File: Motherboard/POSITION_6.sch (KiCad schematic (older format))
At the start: 31 parts, among them Q24 MOSFET_N_(2N7002P,215), Q25 MOSFET_N_(2N7002P,215), Q26 MOSFET_N_(FDMA430NZ), Q27 MOSFET_P_(BS250FTA)

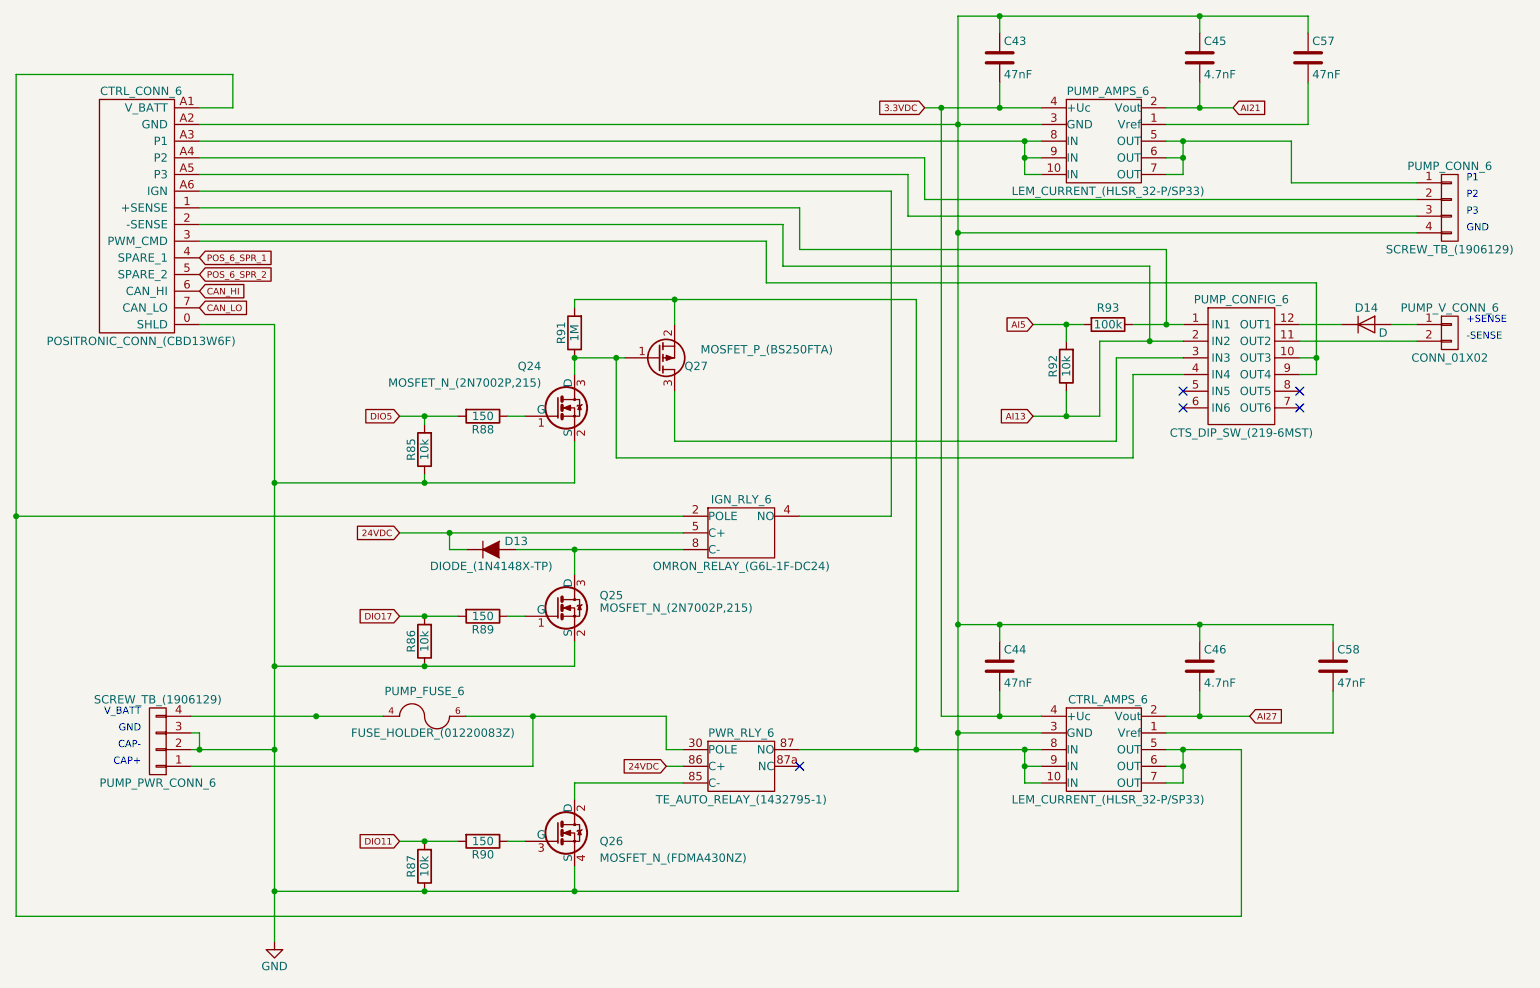
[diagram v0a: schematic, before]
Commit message: - Refer to Google Drive BOM for list of changes for v1.1 - Create drawing for Hella BLDC controller plate.
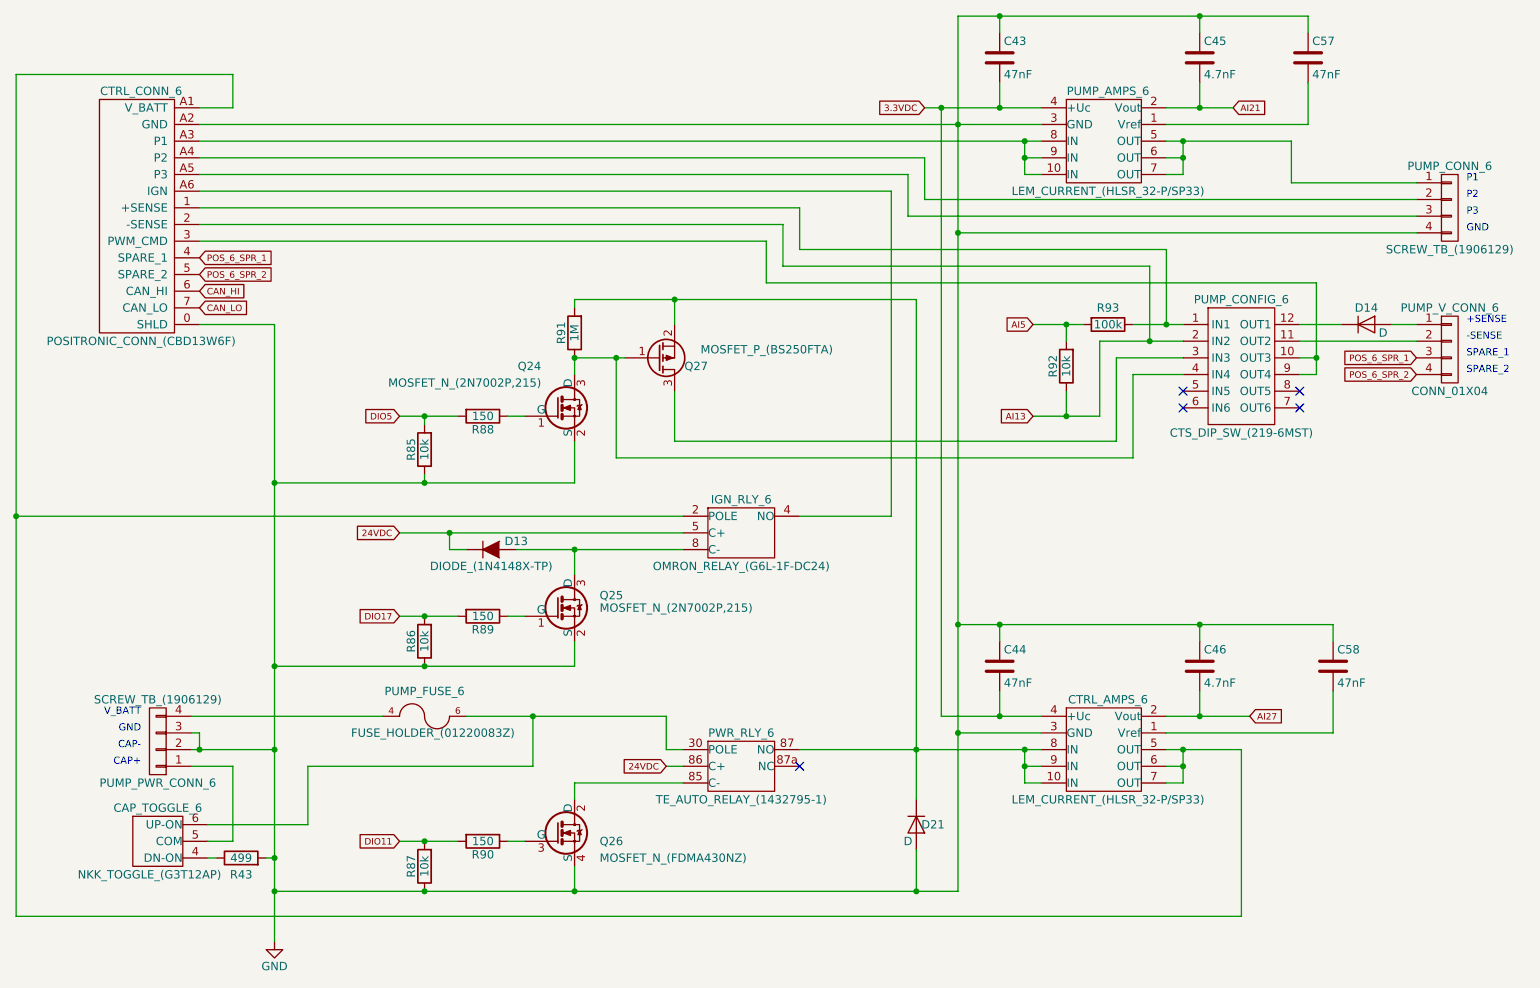
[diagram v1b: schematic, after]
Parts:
- removed PUMP_V_CONN_6: CONN_01X02, Smart_Tank:PHNX_TB_SCREW_2_POS_(1729128), symbol CONN_01X02
- added CAP_TOGGLE_6: NKK_TOGGLE_(G3T12AP), Smart_Tank:NKK_TOGGLE_(G3T12AP), symbol NKK_TOGGLE_(G3T12AP)
- added D21: D, Diodes_SMD:D_SOD-123, symbol D
- added PUMP_V_CONN_6: CONN_01X04, Smart_Tank:PHNX_TB_SCREW_4_POS_(1729144), symbol CONN_01X04
- added R43: 499, Resistors_SMD:R_1206, symbol R
- D14: footprint Diodes_SMD:SOD-523 -> Diodes_SMD:SOD-123
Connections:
- net GND: now also D21.2 (A), R43.2
- net POS_6_SPR_1: now also PUMP_V_CONN_6.3 (P3)
- net POS_6_SPR_2: now also PUMP_V_CONN_6.4 (P4)
- net at PUMP_FUSE_6.6, PUMP_FUSE_6.7, PWR_RLY_6.30 (POLE): now also CAP_TOGGLE_6.6 (UP-ON); no longer PUMP_PWR_CONN_6.1 (P1)
- net at CTRL_AMPS_6.10 (IN), CTRL_AMPS_6.8 (IN), CTRL_AMPS_6.9 (IN)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: now also D21.1 (K)
- net at PUMP_CONFIG_6.11 (OUT2): now also PUMP_V_CONN_6.2 (P2)
- net at D14.2 (A): now also PUMP_V_CONN_6.1 (P1)
- new net: CAP_TOGGLE_6.5 (COM), PUMP_PWR_CONN_6.1 (P1)
- new net: CAP_TOGGLE_6.4 (DN-ON), R43.1
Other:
- note added: "SPARE_1"
- note added: "SPARE_2"
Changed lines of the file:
@@
 CAP+
 $Comp
-L GND #PWR026
+L GND #PWR027
 U 1 1 57A945C3
 P 2950 6350
-F 0 "#PWR026" H 2950 6100 50  0001 C CNN
+F 0 "#PWR027" H 2950 6100 50  0001 C CNN
 F 1 "GND" H 2950 6200 50  0000 C CNN
 F 2 "" H 2950 6350 50  0000 C CNN
@@
 	1    0    0    -1
 $EndComp
-$Comp
-L CONN_01X02 PUMP_V_CONN_6
-U 1 1 57A9467F
-P 10000 2700
-F 0 "PUMP_V_CONN_6" H 10000 2850 50  0000 C CNN
-F 1 "CONN_01X02" H 10000 2550 50  0000 C CNN
-F 2 "Smart_Tank:PHNX_TB_SCREW_2_POS_(1729128)" H 10000 2700 50  0001 C CNN
-F 3 "" H 10000 2700 50  0000 C CNN
-	1    10000 2700
-	1    0    0    -1
-$EndComp
 Text Notes 10100 2650 0    43   ~ 0
 +SENSE
@@
 	2500 5100 2500 5200
 Connection ~ 2500 5200
-Wire Wire Line
-	4500 5300 2450 5300
 Connection ~ 4500 5000
 Wire Wire Line
@@
 	4750 2500 6800 2500
 Wire Wire Line
-	6800 2500 6800 5200
+	6800 2500 6800 5500
 Connection ~ 6800 5200
 Wire Wire Line
@@
 	2950 4700 4750 4700
 Connection ~ 3850 4700
-Connection ~ 3200 5000
 Connection ~ 2950 6050
 Wire Wire Line
@@
 F 0 "D14" H 9500 2750 50  0000 C CNN
 F 1 "D" H 9600 2600 50  0000 C CNN
-F 2 "Diodes_SMD:SOD-523" H 9500 2650 50  0001 C CNN
+F 2 "Diodes_SMD:SOD-123" H 9500 2650 50  0001 C CNN
 F 3 "" H 9500 2650 50  0000 C CNN
 	1    9500 2650
@@
 	9300 4450 9300 4550
 Connection ~ 8500 4450
+$Comp
+L NKK_TOGGLE_(G3T12AP) CAP_TOGGLE_6
+U 1 1 5976DF6C
+P 2250 5750
+F 0 "CAP_TOGGLE_6" H 2250 5950 50  0000 C CNN
+F 1 "NKK_TOGGLE_(G3T12AP)" H 2200 5550 50  0000 C CNN
+F 2 "Smart_Tank:NKK_TOGGLE_(G3T12AP)" H 2250 4550 50  0001 C CNN
+F 3 "" H 2250 4550 50  0000 C CNN
+	1    2250 5750
+	1    0    0    -1
+$EndComp
+Wire Wire Line
+	2450 5300 2700 5300
+Wire Wire Line
+	3150 5300 4500 5300
+$Comp
+L D D21
+U 1 1 5976EE02
+P 6800 5650
+F 0 "D21" V 6800 5750 50  0000 C CNN
+F 1 "D" V 6900 5600 50  0000 C CNN
+F 2 "Diodes_SMD:D_SOD-123" H 6800 5650 50  0001 C CNN
+F 3 "" H 6800 5650 50  0000 C CNN
+	1    6800 5650
+	0    1    1    0
+$EndComp
+Wire Wire Line
+	6800 5800 6800 6050
+Connection ~ 6800 6050
+$Comp
+L R R43
+U 1 1 5978DEAB
+P 2750 5850
+F 0 "R43" V 2650 5850 50  0000 C CNN
+F 1 "499" V 2750 5850 50  0000 C CNN
+F 2 "Resistors_SMD:R_1206" V 2680 5850 50  0001 C CNN
+F 3 "" H 2750 5850 50  0000 C CNN
+	1    2750 5850
+	0    -1   -1   0
+$EndComp
+Wire Wire Line
+	2550 5750 2700 5750
+Wire Wire Line
+	2700 5750 2700 5300
+Wire Wire Line
+	2550 5650 3150 5650
+Wire Wire Line
+	3150 5650 3150 5300
+Wire Wire Line
+	2600 5850 2550 5850
+Wire Wire Line
+	2900 5850 2950 5850
+Connection ~ 2950 5850
+$Comp
+L CONN_01X04 PUMP_V_CONN_6
+U 1 1 5979C896
+P 10000 2800
+F 0 "PUMP_V_CONN_6" H 10000 3050 50  0000 C CNN
+F 1 "CONN_01X04" H 10000 2550 50  0000 C CNN
+F 2 "Smart_Tank:PHNX_TB_SCREW_4_POS_(1729144)" H 10000 2800 50  0001 C CNN
+F 3 "" H 10000 2800 50  0001 C CNN
+	1    10000 2800
+	1    0    0    -1
+$EndComp
+Text GLabel 9800 2850 0    39   Input ~ 0
+POS_6_SPR_1
+Text GLabel 9800 2950 0    39   Input ~ 0
+POS_6_SPR_2
+Text Notes 10100 2850 0    43   ~ 0
+SPARE_1
+Text Notes 10100 2950 0    43   ~ 0
+SPARE_2
 $EndSCHEMATC

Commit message: - Created Modbus Adapter.
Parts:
- C43, C44, C45, C46, C57, C58: symbol C -> Smart-Tank-Motherboard-rescue:C
- CAP_TOGGLE_6: symbol NKK_TOGGLE_(G3T12AP) -> Smart-Tank-Motherboard-rescue:NKK_TOGGLE_(G3T12AP)
- CTRL_AMPS_6, PUMP_AMPS_6: symbol LEM_CURRENT_(HLSR_32-P/SP33) -> Smart-Tank-Motherboard-rescue:LEM_CURRENT_(HLSR_32-P_SP33)
- CTRL_CONN_6: symbol POSITRONIC_CONN_(CBD13W6F) -> Smart-Tank-Motherboard-rescue:POSITRONIC_CONN_(CBD13W6F)
- D13: symbol DIODE_(1N4148X-TP) -> Smart-Tank-Motherboard-rescue:DIODE_(1N4148X-TP)
- D14, D21: symbol D -> Smart-Tank-Motherboard-rescue:D
- IGN_RLY_6: symbol OMRON_RELAY_(G6L-1F-DC24) -> Smart-Tank-Motherboard-rescue:OMRON_RELAY_(G6L-1F-DC24)
- PUMP_CONFIG_6: symbol CTS_DIP_SW_(219-6MST) -> Smart-Tank-Motherboard-rescue:CTS_DIP_SW_(219-6MST)
- PUMP_CONN_6, PUMP_PWR_CONN_6: symbol SCREW_TB_(1906129) -> Smart-Tank-Motherboard-rescue:SCREW_TB_(1906129)
- PUMP_FUSE_6: symbol FUSE_HOLDER_(01220083Z) -> Smart-Tank-Motherboard-rescue:FUSE_HOLDER_(01220083Z)
- PUMP_V_CONN_6: symbol CONN_01X04 -> Smart-Tank-Motherboard-rescue:CONN_01X04
- PWR_RLY_6: symbol TE_AUTO_RELAY_(1432795-1) -> Smart-Tank-Motherboard-rescue:TE_AUTO_RELAY_(1432795-1)
- Q24, Q25: symbol MOSFET_N_(2N7002P,215) -> Smart-Tank-Motherboard-rescue:MOSFET_N_(2N7002P,215)
- Q26: symbol MOSFET_N_(FDMA430NZ) -> Smart-Tank-Motherboard-rescue:MOSFET_N_(FDMA430NZ)
- Q27: symbol MOSFET_P_(BS250FTA) -> Smart-Tank-Motherboard-rescue:MOSFET_P_(BS250FTA)
- R43, R85, R86, R87, R88, R89, R90, R91, R92, R93: symbol R -> Smart-Tank-Motherboard-rescue:R
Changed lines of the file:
@@
-EESchema Schematic File Version 2
-LIBS:Smart Tank Motherboard-rescue
-LIBS:power
-LIBS:device
-LIBS:transistors
-LIBS:conn
-LIBS:linear
-LIBS:regul
-LIBS:74xx
-LIBS:cmos4000
-LIBS:adc-dac
-LIBS:memory
-LIBS:xilinx
-LIBS:microcontrollers
-LIBS:dsp
-LIBS:microchip
-LIBS:analog_switches
-LIBS:motorola
-LIBS:texas
-LIBS:intel
-LIBS:audio
-LIBS:interface
-LIBS:digital-audio
-LIBS:philips
-LIBS:display
-LIBS:cypress
-LIBS:siliconi
-LIBS:opto
-LIBS:atmel
-LIBS:contrib
-LIBS:valves
+EESchema Schematic File Version 4
 LIBS:Smart Tank Motherboard-cache
-EELAYER 25 0
+EELAYER 29 0
 EELAYER END
 $Descr A4 11693 8268
@@
 $EndDescr
 $Comp
-L R R90
+L Smart-Tank-Motherboard-rescue:R R90
 U 1 1 57A945A9
 P 4200 5750
@@
 $EndComp
 $Comp
-L R R87
+L Smart-Tank-Motherboard-rescue:R R87
 U 1 1 57A945B0
 P 3850 5900
@@
 $EndComp
 $Comp
-L SCREW_TB_(1906129) PUMP_PWR_CONN_6
+L Smart-Tank-Motherboard-rescue:SCREW_TB_(1906129) PUMP_PWR_CONN_6
 U 1 1 57A945B8
 P 2250 5150
@@
 CAP+
 $Comp
-L GND #PWR027
+L Smart-Tank-Motherboard-rescue:GND #PWR027
 U 1 1 57A945C3
 P 2950 6350
@@
 $EndComp
 $Comp
-L SCREW_TB_(1906129) PUMP_CONN_6
+L Smart-Tank-Motherboard-rescue:SCREW_TB_(1906129) PUMP_CONN_6
 U 1 1 57A945D8
 P 10000 1950
@@
 GND
 $Comp
-L POSITRONIC_CONN_(CBD13W6F) CTRL_CONN_6
+L Smart-Tank-Motherboard-rescue:POSITRONIC_CONN_(CBD13W6F) CTRL_CONN_6
 U 1 1 57A945E3
 P 2150 1900
@@
 $EndComp
 $Comp
-L FUSE_HOLDER_(01220083Z) PUMP_FUSE_6
+L Smart-Tank-Motherboard-rescue:FUSE_HOLDER_(01220083Z) PUMP_FUSE_6
 U 1 1 57A945EA
 P 3850 5000
@@
 $EndComp
 $Comp
-L MOSFET_N_(FDMA430NZ) Q26
+L Smart-Tank-Motherboard-rescue:MOSFET_N_(FDMA430NZ) Q26
 U 1 1 57A945F1
 P 4650 5700
@@
 $EndComp
 $Comp
-L TE_AUTO_RELAY_(1432795-1) PWR_RLY_6
+L Smart-Tank-Motherboard-rescue:TE_AUTO_RELAY_(1432795-1) PWR_RLY_6
 U 1 1 57A945F8
 P 5650 5400
@@
 AI27
 $Comp
-L OMRON_RELAY_(G6L-1F-DC24) IGN_RLY_6
+L Smart-Tank-Motherboard-rescue:OMRON_RELAY_(G6L-1F-DC24) IGN_RLY_6
 U 1 1 57A94604
 P 5650 4000
@@
 $EndComp
 $Comp
-L MOSFET_N_(2N7002P,215) Q25
+L Smart-Tank-Motherboard-rescue:MOSFET_N_(2N7002P,215) Q25
 U 1 1 57A9460B
 P 4650 4350
@@
 $EndComp
 $Comp
-L R R89
+L Smart-Tank-Motherboard-rescue:R R89
 U 1 1 57A94612
 P 4200 4400
@@
 $EndComp
 $Comp
-L R R86
+L Smart-Tank-Motherboard-rescue:R R86
 U 1 1 57A94619
 P 3850 4550
@@
 CAN_LO
 $Comp
-L DIODE_(1N4148X-TP) D13
+L Smart-Tank-Motherboard-rescue:DIODE_(1N4148X-TP) D13
 U 1 1 57A94624
 P 4250 4000
@@
 POS_6_SPR_2
 $Comp
-L MOSFET_N_(2N7002P,215) Q24
+L Smart-Tank-Motherboard-rescue:MOSFET_N_(2N7002P,215) Q24
 U 1 1 57A9462D
 P 4650 3150
@@
 $EndComp
 $Comp
-L MOSFET_P_(BS250FTA) Q27
+L Smart-Tank-Motherboard-rescue:MOSFET_P_(BS250FTA) Q27
 U 1 1 57A94634
 P 5250 2850
@@
 $EndComp
 $Comp
-L R R88
+L Smart-Tank-Motherboard-rescue:R R88
 U 1 1 57A9463B
 P 4200 3200
@@
 $EndComp
 $Comp
-L R R91
+L Smart-Tank-Motherboard-rescue:R R91
 U 1 1 57A94642
 P 4750 2700
@@
 DIO5
 $Comp
-L R R85
+L Smart-Tank-Motherboard-rescue:R R85
 U 1 1 57A9464A
 P 3850 3400
@@
 NoConn ~ 6100 5300
 $Comp
-L C C45
+L Smart-Tank-Motherboard-rescue:C C45
 U 1 1 57A9465C
 P 8500 1050
@@
 $EndComp
 $Comp
-L C C43
+L Smart-Tank-Motherboard-rescue:C C43
 U 1 1 57A94663
 P 7300 1050
@@
 $EndComp
 $Comp
-L C C46
+L Smart-Tank-Motherboard-rescue:C C46
 U 1 1 57A9466A
 P 8500 4700
@@
 $EndComp
 $Comp
-L C C44
+L Smart-Tank-Motherboard-rescue:C C44
 U 1 1 57A94671
 P 7300 4700
@@
 $EndComp
 $Comp
-L CTS_DIP_SW_(219-6MST) PUMP_CONFIG_6
+L Smart-Tank-Motherboard-rescue:CTS_DIP_SW_(219-6MST) PUMP_CONFIG_6
 U 1 1 57A94678
 P 8750 2900
@@
 NoConn ~ 8400 3150
 $Comp
-L R R92
+L Smart-Tank-Motherboard-rescue:R R92
 U 1 1 57A9468C
 P 7700 2900
@@
 $EndComp
 $Comp
-L R R93
+L Smart-Tank-Motherboard-rescue:R R93
 U 1 1 57A94693
 P 7950 2650
@@
 	4750 2550 4750 2500
 $Comp
-L D D14
+L Smart-Tank-Motherboard-rescue:D D14
 U 1 1 57A94751
 P 9500 2650
@@
 	9650 2650 9800 2650
 $Comp
-L LEM_CURRENT_(HLSR_32-P/SP33) PUMP_AMPS_6
+L Smart-Tank-Motherboard-rescue:LEM_CURRENT_(HLSR_32-P_SP33) PUMP_AMPS_6
 U 1 1 57B74ABE
 P 7800 1550
@@
 $EndComp
 $Comp
-L LEM_CURRENT_(HLSR_32-P/SP33) CTRL_AMPS_6
+L Smart-Tank-Motherboard-rescue:LEM_CURRENT_(HLSR_32-P_SP33) CTRL_AMPS_6
 U 1 1 57B77311
 P 7800 5200
@@
 Connection ~ 2950 3600
 $Comp
-L C C57
+L Smart-Tank-Motherboard-rescue:C C57
 U 1 1 57D20C93
 P 9150 1050
@@
 Connection ~ 8500 800
 $Comp
-L C C58
+L Smart-Tank-Motherboard-rescue:C C58
 U 1 1 57D211BE
 P 9300 4700
@@
 Connection ~ 8500 4450
 $Comp
-L NKK_TOGGLE_(G3T12AP) CAP_TOGGLE_6
+L Smart-Tank-Motherboard-rescue:NKK_TOGGLE_(G3T12AP) CAP_TOGGLE_6
 U 1 1 5976DF6C
 P 2250 5750
@@
 	3150 5300 4500 5300
 $Comp
-L D D21
+L Smart-Tank-Motherboard-rescue:D D21
 U 1 1 5976EE02
 P 6800 5650
@@
 Connection ~ 6800 6050
 $Comp
-L R R43
+L Smart-Tank-Motherboard-rescue:R R43
 U 1 1 5978DEAB
 P 2750 5850
@@
 Connection ~ 2950 5850
 $Comp
-L CONN_01X04 PUMP_V_CONN_6
+L Smart-Tank-Motherboard-rescue:CONN_01X04 PUMP_V_CONN_6
 U 1 1 5979C896
 P 10000 2800
